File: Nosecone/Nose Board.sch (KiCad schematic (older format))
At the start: 48 parts, among them J1 Conn_01x02, J2 Conn_02x04_Odd_Even, J3 Conn_02x03_Odd_Even, J4 Conn_Coaxial, J5 Conn_01x02, Q1 Q_PMOS_DGS, Q2 Q_PMOS_DGS, U1 RS485_converter_ISL83488, U10 MS5803-14BA, U11 MS5803-14BA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

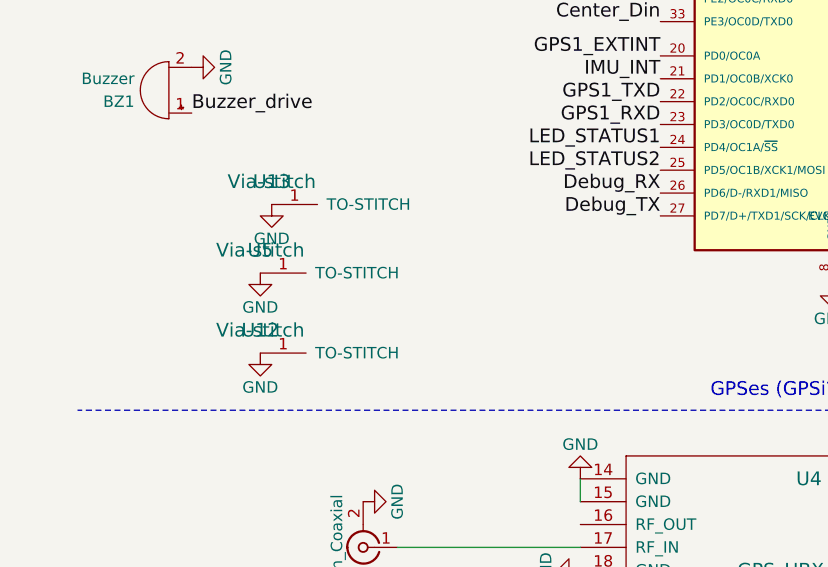
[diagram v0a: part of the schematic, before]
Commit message: Actually fixed the DRC issues. Oops
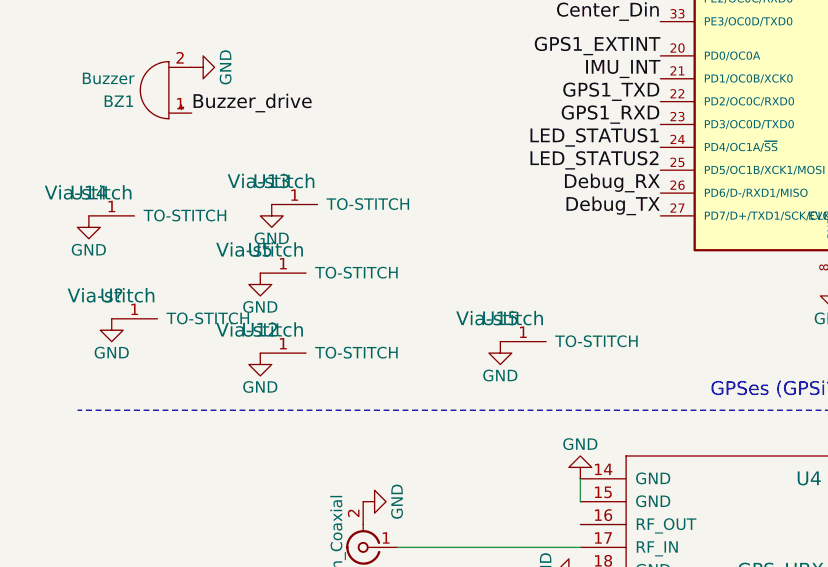
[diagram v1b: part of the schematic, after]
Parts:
- added U14, U15, U?: Via-stitch, Misc components:Small-via, symbol Via-stitch
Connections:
- net GND: now also U14.1 (TO-STITCH), U15.1 (TO-STITCH), U?.1 (TO-STITCH)

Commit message: Better routing
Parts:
- added U17, U18, U19, U20: Via-stitch, Misc components:4_40_through_hole, symbol Via-stitch
- gave numbers to parts that had none: 1
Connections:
- net RS422in+: now reaches J2.6 (Pin_6)
- net RS422in+: now also U1.6 (Z); no longer U1.5 (Y)
- net RS422out-: now reaches J2.5 (Pin_5)
- net RS422out-: now also U1.7 (B); no longer U1.6 (Z)
- net RS422in-: now reaches J2.4 (Pin_4)
- net RS422in-: now also U1.5 (Y); no longer U1.7 (B)
- net RS422out+: now reaches J2.3 (Pin_3), U1.8 (A)
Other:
- moved on the sheet: U1

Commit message: Fixed via and board outline issues
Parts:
- U12, U13, U14, U15, U16, U5: footprint Misc components:Small-via -> Misc components:small-via
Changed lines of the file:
@@
 F 0 "U5" H 1500 4400 60  0000 C CNN
 F 1 "Via-stitch" H 1500 4400 60  0000 C CNN
-F 2 "Misc components:Small-via" H 1500 4400 60  0001 C CNN
+F 2 "Misc components:small-via" H 1500 4400 60  0001 C CNN
 F 3 "" H 1500 4400 60  0001 C CNN
 	1    1500 4400
@@
 F 0 "U12" H 1500 4750 60  0000 C CNN
 F 1 "Via-stitch" H 1500 4750 60  0000 C CNN
-F 2 "Misc components:Small-via" H 1500 4750 60  0001 C CNN
+F 2 "Misc components:small-via" H 1500 4750 60  0001 C CNN
 F 3 "" H 1500 4750 60  0001 C CNN
 	1    1500 4750
@@
 F 0 "U13" H 1550 4100 60  0000 C CNN
 F 1 "Via-stitch" H 1550 4100 60  0000 C CNN
-F 2 "Misc components:Small-via" H 1550 4100 60  0001 C CNN
+F 2 "Misc components:small-via" H 1550 4100 60  0001 C CNN
 F 3 "" H 1550 4100 60  0001 C CNN
 	1    1550 4100
@@
 F 0 "U14" H 750 4150 60  0000 C CNN
 F 1 "Via-stitch" H 750 4150 60  0000 C CNN
-F 2 "Misc components:Small-via" H 750 4150 60  0001 C CNN
+F 2 "Misc components:small-via" H 750 4150 60  0001 C CNN
 F 3 "" H 750 4150 60  0001 C CNN
 	1    750  4150
@@
 F 0 "U15" H 2550 4700 60  0000 C CNN
 F 1 "Via-stitch" H 2550 4700 60  0000 C CNN
-F 2 "Misc components:Small-via" H 2550 4700 60  0001 C CNN
+F 2 "Misc components:small-via" H 2550 4700 60  0001 C CNN
 F 3 "" H 2550 4700 60  0001 C CNN
 	1    2550 4700
@@
 F 0 "U16" H 850 4600 60  0000 C CNN
 F 1 "Via-stitch" H 850 4600 60  0000 C CNN
-F 2 "Misc components:Small-via" H 850 4600 60  0001 C CNN
+F 2 "Misc components:small-via" H 850 4600 60  0001 C CNN
 F 3 "" H 850 4600 60  0001 C CNN
 	1    850  4600
